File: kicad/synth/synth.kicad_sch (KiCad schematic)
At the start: 2 parts

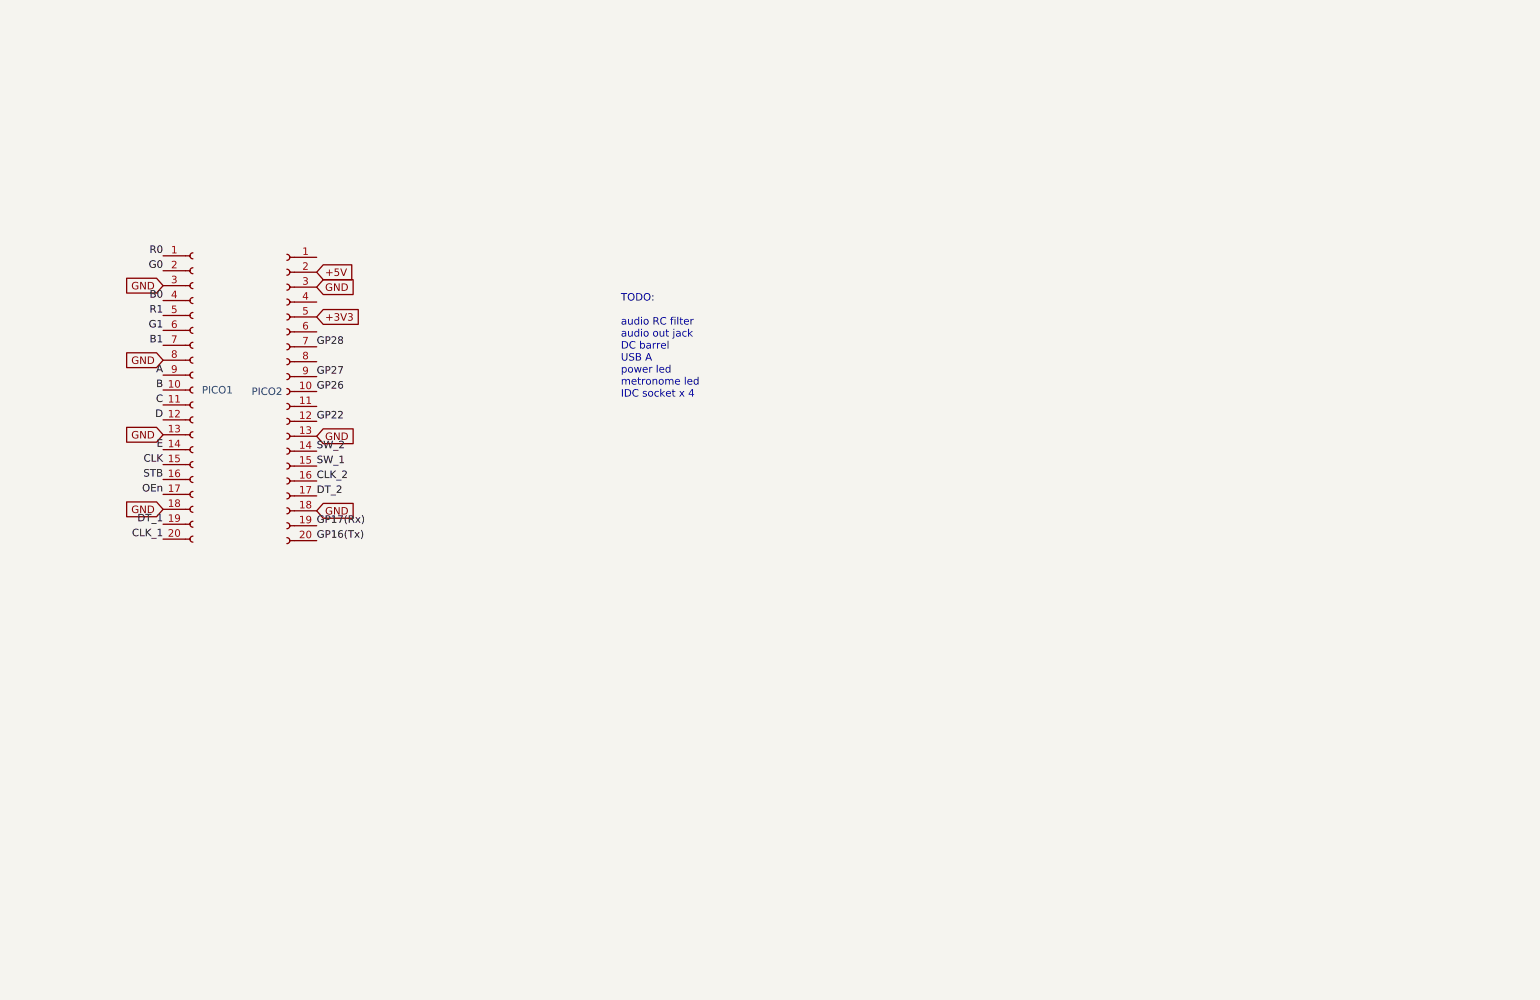
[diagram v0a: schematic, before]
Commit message: sketch out LM386 amp
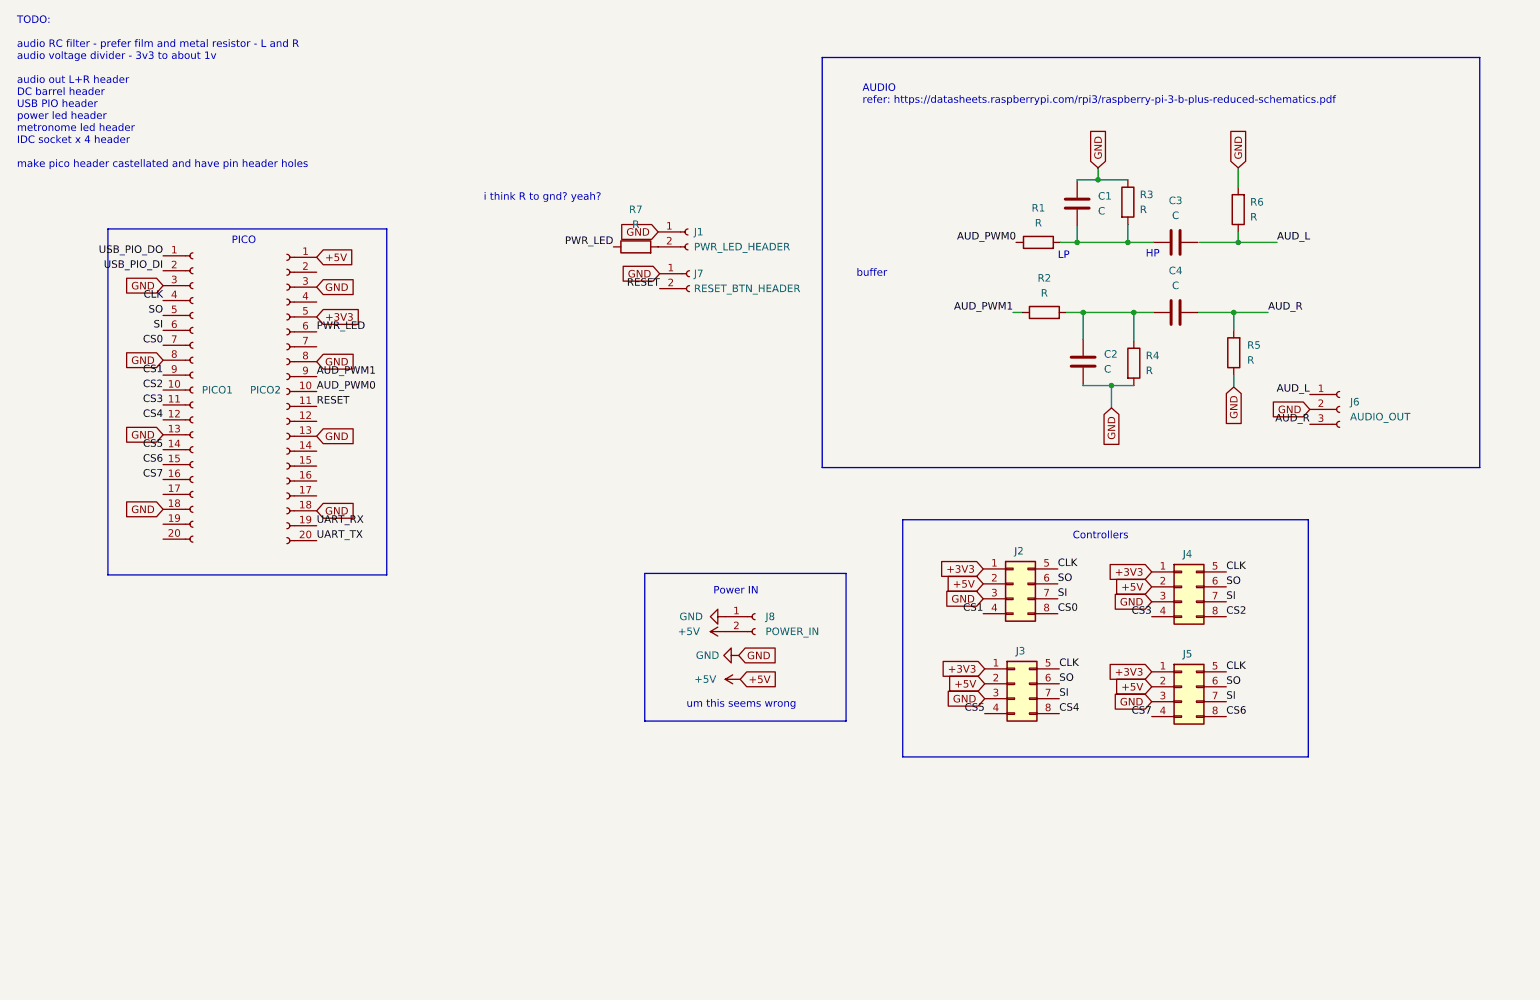
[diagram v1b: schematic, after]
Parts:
- added C1, C2, C3, C4: C, Capacitor_SMD:C_0805_2012Metric_Pad1.18x1.45mm_HandSolder, symbol Device:C
- added J1: PWR_LED_HEADER, Connector_PinHeader_1.00mm:PinHeader_1x02_P1.00mm_Vertical, symbol Connector:Conn_01x02_Socket
- added J2, J3, J4, J5: Conn_02x04_Top_Bottom, Connector_IDC:IDC-Header_2x04_P2.54mm_Vertical_SMD, symbol Connector_Generic:Conn_02x04_Top_Bottom
- added J6: AUDIO_OUT, Connector_PinHeader_1.00mm:PinHeader_1x03_P1.00mm_Vertical, symbol Connector:Conn_01x03_Socket
- added J7: RESET_BTN_HEADER, Connector_PinHeader_1.00mm:PinHeader_1x02_P1.00mm_Vertical, symbol Connector:Conn_01x02_Socket
- added J8: POWER_IN, Connector_PinHeader_1.00mm:PinHeader_1x02_P1.00mm_Vertical, symbol Connector:Conn_01x02_Socket
- added R1, R2, R3, R4, R5, R6, R7: R, Resistor_SMD:R_0805_2012Metric_Pad1.20x1.40mm_HandSolder, symbol Device:R
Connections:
- net B0 is gone; now on net CLK: PICO1.4 (Pin_4)
- net +3V3: now also J2.1 (Pin_1), J3.1 (Pin_1), J4.1 (Pin_1), J5.1 (Pin_1)
- net +5V: now also PICO2.1 (Pin_1), J2.2 (Pin_2), J3.2 (Pin_2), J4.2 (Pin_2), J5.2 (Pin_2), J8.2 (Pin_2); no longer PICO2.2 (Pin_2)
- net CLK: now also J2.5 (Pin_5), J3.5 (Pin_5), J4.5 (Pin_5), J5.5 (Pin_5); no longer PICO1.15 (Pin_15)
- net GND: now also PICO2.8 (Pin_8), C1.1, C2.2, J1.1 (Pin_1), J2.3 (Pin_3), J3.3 (Pin_3), J4.3 (Pin_3), J5.3 (Pin_3), J6.2 (Pin_2), J7.1 (Pin_1), J8.1 (Pin_1), R3.1, R4.2, R5.1, R6.2
- net RESET: now reaches PICO2.11 (Pin_11)
- net RESET: now also J7.2 (Pin_2)
- net PWR_LED: now reaches PICO2.6 (Pin_6)
- net PWR_LED: now also R7.1
- net A renamed CS1
- net CS1: now also J2.4 (Pin_4)
- net B renamed CS2
- net CS2: now also J4.8 (Pin_8)
- net B1 renamed CS0
- net CS0: now also J2.8 (Pin_8)
- net C renamed CS3
- net CS3: now also J4.4 (Pin_4)
- net CLK_1: no longer names the net of PICO1.20 (Pin_20)
- net CLK_2: no longer names the net of PICO2.16 (Pin_16)
- net D renamed CS4
- net CS4: now also J3.8 (Pin_8)
- net DT_1: no longer names the net of PICO1.19 (Pin_19)
- net DT_2: no longer names the net of PICO2.17 (Pin_17)
- net E renamed CS5
- net CS5: now also J3.4 (Pin_4)
- net G0 renamed USB_PIO_DI
- net G1 renamed SI
- net SI: now also J2.7 (Pin_7), J3.7 (Pin_7), J4.7 (Pin_7), J5.7 (Pin_7)
- net GP16(Tx) renamed UART_TX
- net GP17(Rx) renamed UART_RX
- net GP22: no longer names the net of PICO2.12 (Pin_12)
- net GP26 renamed AUD_PWM0
- net AUD_PWM0: now also R1.1
- net GP27 renamed AUD_PWM1
- net AUD_PWM1: now also R2.1
- net GP28: no longer names the net of PICO2.7 (Pin_7)
- net OEn: no longer names the net of PICO1.17 (Pin_17)
- net R0 renamed USB_PIO_DO
- net R1 renamed SO
- net SO: now also J2.6 (Pin_6), J3.6 (Pin_6), J4.6 (Pin_6), J5.6 (Pin_6)
- net STB renamed CS7
- net CS7: now also J5.4 (Pin_4)
- net SW_1: no longer names the net of PICO2.15 (Pin_15)
- net SW_2: no longer names the net of PICO2.14 (Pin_14)
- new net: C1.2, C3.1, R1.2, R3.2
- new net: C2.1, C4.1, R2.2, R4.1
- new net: J1.2 (Pin_2), R7.2
- new net AUD_L: J6.1 (Pin_1), R6.1
- new net AUD_R: C4.2, J6.3 (Pin_3), R5.2
- new net CS6: J5.8 (Pin_8), PICO1.15 (Pin_15)
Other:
- note added: "AUDIO refer: https://datasheets.raspberrypi.com/rpi3/raspberry-pi-3-b-plus-reduced-schematics.pdf"
- note added: "Controllers"
- note added: "HP"
- note added: "LP"
- note added: "PICO"
- note added: "Power IN"
- note added: "TODO: audio RC filter - prefer film and metal resistor - L and R audio voltage divider - 3v3 to about 1v audio out L+R header DC barrel header USB PIO header power led header metronome led header IDC socket x 4 header make pico header castellated and have pin header holes"
- note added: "buffer"
- note added: "i think R to gnd? yeah?"
- note added: "um this seems wrong"
- note removed: "TODO: audio RC filter audio out jack DC barrel USB A power led metronome led IDC socket x 4"

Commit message: fix button behaviour now I have a PCB
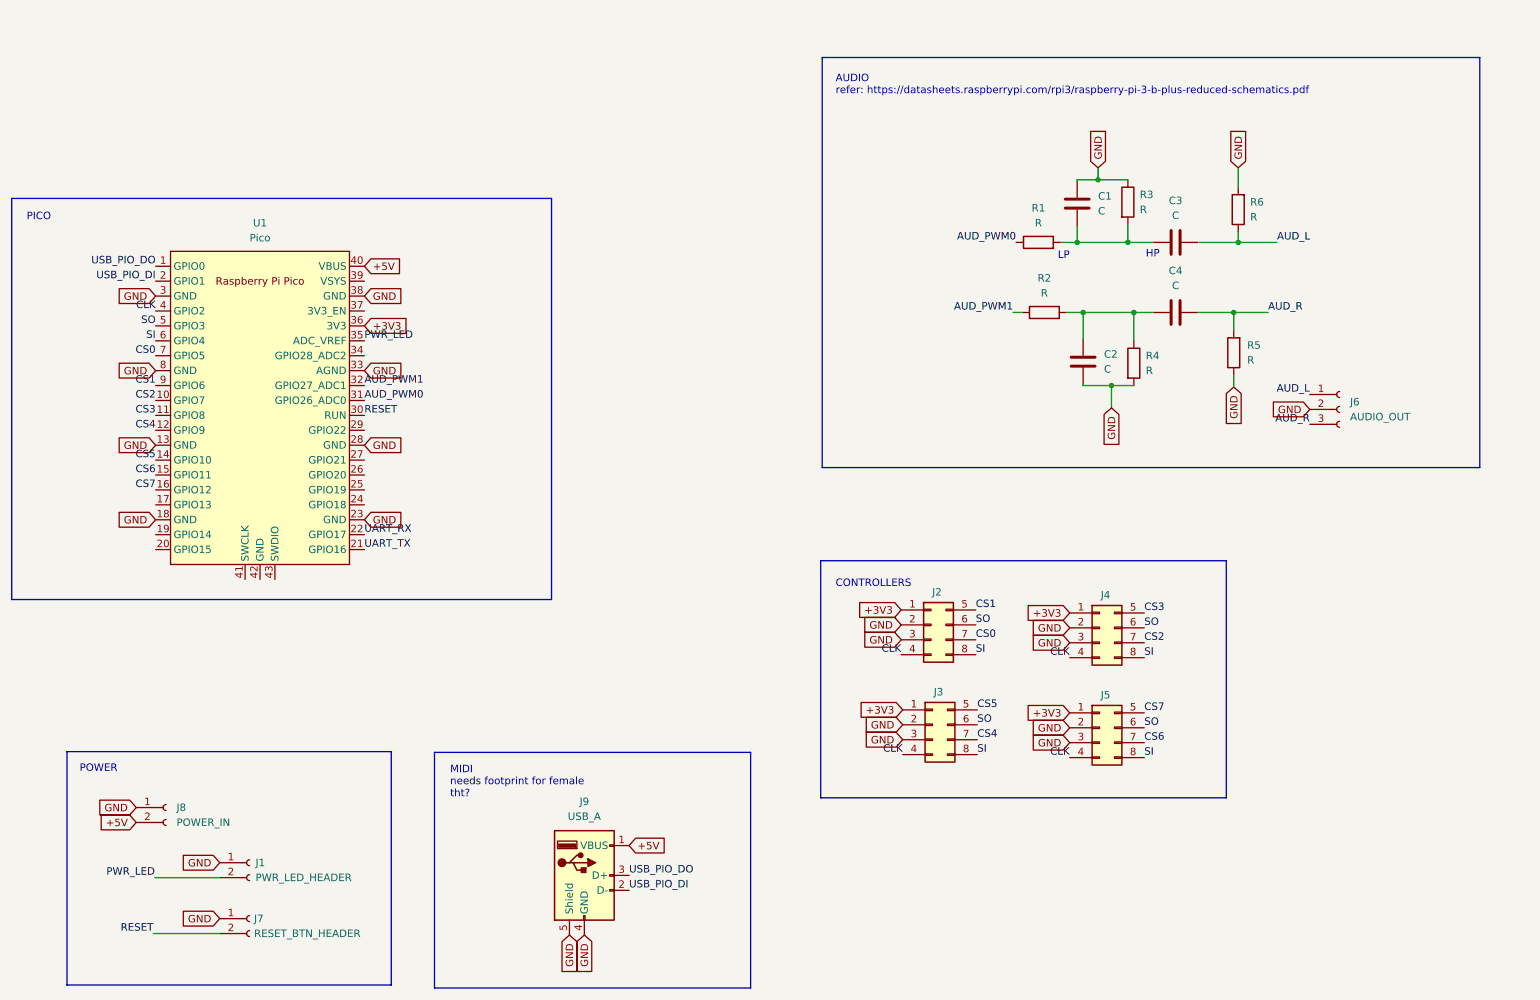
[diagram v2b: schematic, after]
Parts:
- removed PICO1: PICO_L, Connector_PinSocket_2.54mm:PinSocket_1x20_P2.54mm_Vertical, symbol Connector:Conn_01x20_Socket
- removed PICO2: PICO_R, Connector_PinSocket_2.54mm:PinSocket_1x20_P2.54mm_Vertical, symbol Connector:Conn_01x20_Socket
- removed R7: R, Resistor_SMD:R_0805_2012Metric_Pad1.20x1.40mm_HandSolder, symbol Device:R
- added J9: USB_A, Connector_USB:USB_A_CNCTech_1001-011-01101_Horizontal, symbol Connector:USB_A
- added U1: Pico, MCU_RaspberryPi_and_Boards:RPi_Pico_SMD_TH, symbol MCU_RaspberryPi_and_Boards:Pico
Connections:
- net +3V3: now also U1.36 (3V3)
- net +5V: now also J9.1 (VBUS), U1.40 (VBUS); no longer J2.2 (Pin_2), J3.2 (Pin_2), J4.2 (Pin_2), J5.2 (Pin_2)
- net AUD_PWM0: now also U1.31 (GPIO26_ADC0)
- net AUD_PWM1: now also U1.32 (GPIO27_ADC1)
- net CLK: now also J2.4 (Pin_4), J3.4 (Pin_4), J4.4 (Pin_4), J5.4 (Pin_4), U1.4 (GPIO2); no longer J2.5 (Pin_5), J3.5 (Pin_5), J4.5 (Pin_5), J5.5 (Pin_5)
- net CS0: now also J2.7 (Pin_7), U1.7 (GPIO5); no longer J2.8 (Pin_8)
- net CS1: now also J2.5 (Pin_5), U1.9 (GPIO6); no longer J2.4 (Pin_4)
- net CS2: now also J4.7 (Pin_7), U1.10 (GPIO7); no longer J4.8 (Pin_8)
- net CS3: now also J4.5 (Pin_5), U1.11 (GPIO8); no longer J4.4 (Pin_4)
- net CS4: now also J3.7 (Pin_7), U1.12 (GPIO9); no longer J3.8 (Pin_8)
- net CS5: now also J3.5 (Pin_5), U1.14 (GPIO10); no longer J3.4 (Pin_4)
- net CS6: now also J5.7 (Pin_7), U1.15 (GPIO11); no longer J5.8 (Pin_8)
- net CS7: now also J5.5 (Pin_5), U1.16 (GPIO12); no longer J5.4 (Pin_4)
- net GND: now also J2.2 (Pin_2), J3.2 (Pin_2), J4.2 (Pin_2), J5.2 (Pin_2), J9.4 (GND), J9.5 (Shield), U1.13 (GND), U1.18 (GND), U1.23 (GND), U1.28 (GND), U1.3 (GND), U1.33 (AGND), U1.38 (GND), U1.8 (GND)
- net PWR_LED: now also J1.2 (Pin_2), U1.35 (ADC_VREF)
- net RESET: now also U1.30 (RUN)
- net SI: now also J2.8 (Pin_8), J3.8 (Pin_8), J4.8 (Pin_8), J5.8 (Pin_8), U1.6 (GPIO4); no longer J2.7 (Pin_7), J3.7 (Pin_7), J4.7 (Pin_7), J5.7 (Pin_7)
- net SO: now also U1.5 (GPIO3)
- net UART_RX: now also U1.22 (GPIO17)
- net UART_TX: now also U1.21 (GPIO16)
- net USB_PIO_DI: now also J9.2 (D-), U1.2 (GPIO1)
- net USB_PIO_DO: now also J9.3 (D+), U1.1 (GPIO0)
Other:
- note added: "CONTROLLERS"
- note added: "MIDI needs footprint for female tht?"
- note added: "POWER"
- note removed: "Controllers"
- note removed: "Power IN"
- note removed: "TODO: audio RC filter - prefer film and metal resistor - L and R audio voltage divider - 3v3 to about 1v audio out L+R header DC barrel header USB PIO header power led header metronome led header IDC socket x 4 header make pico header castellated and have pin header holes"
- note removed: "buffer"
- note removed: "i think R to gnd? yeah?"
- note removed: "um this seems wrong"
- moved on the sheet: J1, J2, J3, J4, J5, J7, J8
